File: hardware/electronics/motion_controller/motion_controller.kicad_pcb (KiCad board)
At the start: 2 copper layers, 266.7 x 95.3 mm, 186 parts, among them K1 CONN_3, K10 CONN_3, K11 CONN_3, K12 CONN_3, K13 CONN_3, K14 CONN_3, K15 CONN_3, K2 CONN_3, K3 CONN_3, K4 CONN_3, K5 CONN_3, K6 CONN_3, K7 CONN_3, K8 CONN_3, K9 CONN_3, P1 CONN_2, P10 CONN_4, P11 CONN_4, P12 CONN_4, P13 CONN_2, P14 CONN_2, P15 CONN_2, P16 CONN_2, P17 CONN_2, P18 CONN_2, P19 CONN_2X2, P2 CONN_5X2, P20 CONN_2X2, P21 CONN_2, P22 CONN_2, P23 CONN_2, P24 CONN_2, P25 CONN_2, P26 CONN_2X2, P27 CONN_2, P28 CONN_2, P29 CONN_2, P3 CONN_2X2, P30 CONN_1, P31 CONN_1, P32 CONN_1, P33 CONN_1, P4 CONN_2, P5 CONN_34X2, P6 CONN_4, P7 CONN_4, P8 CONN_4, P9 CONN_4, U1 TEENSY3.X, U10 OP07, U11 OP07, U12 OP07, U13 OP07, U14 OP07, U15 OP07, U16 OP07, U17 MEA1D0512SC, U18 PJRC_SD_CARD, U2 NC7WZ04, U3 NC7WZ16, U4 NC7WZ16, U5 SSR_DC_6PIN, U6 MAX6176AASA+, U7 OP07, U8 OP07, U9 OP07

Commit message: Modified motion controller pcb slightly - made so that only one mounting hole is grounded.
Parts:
- U1: value TEENSY3.X -> TEENSY3.1
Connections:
- P30 pad 1: /GND -> (no net)
- P31 pad 1: /GND -> (no net)
- P32 pad 1: /GND -> (no net)
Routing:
- net /GND: track 789.9 -> 771.2 mm
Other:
- board text added: "ANALOG INPUTS"

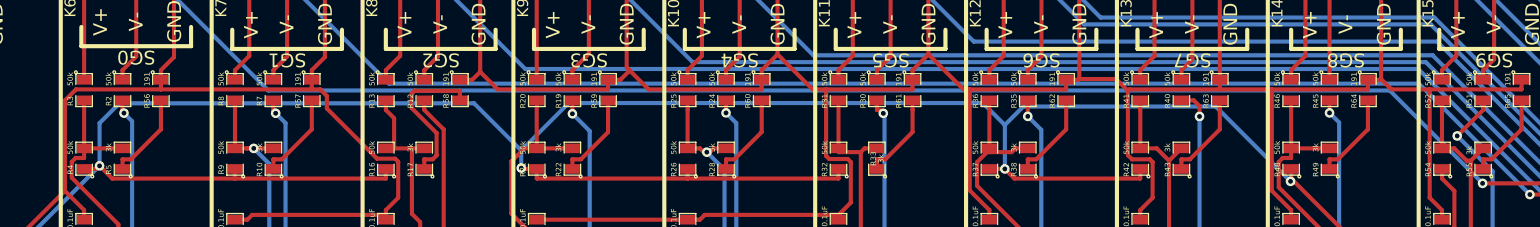
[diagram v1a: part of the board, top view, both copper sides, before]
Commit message: Worked on BOM for motion controller PCB.
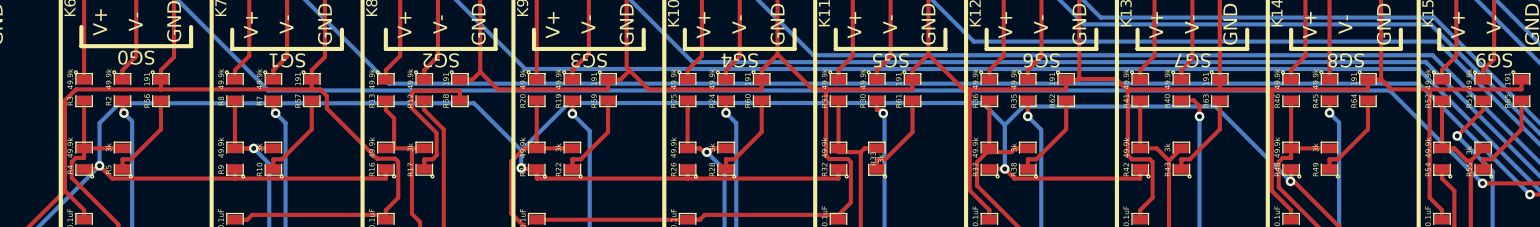
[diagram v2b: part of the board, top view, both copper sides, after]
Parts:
- R12, R13, R16, R19, R2, R20, R21, R24, R25, R26, R3, R30, R31, R32, R35, R36, R37, R4, R40, R41, R42, R45, R46, R48, R51, R52, R54, R7, R8, R9: value 50k -> 49.9k

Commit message: Added sympy derivation of differential amplifier gain for motion controller pcb.
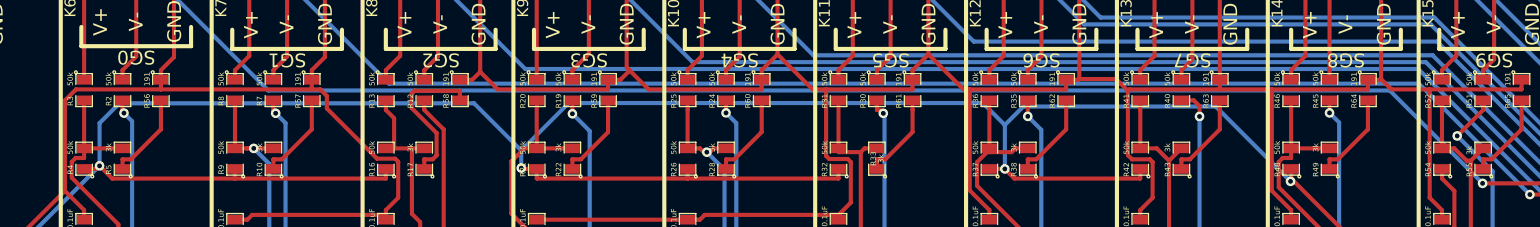
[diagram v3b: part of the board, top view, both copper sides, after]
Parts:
- R12, R13, R16, R19, R2, R20, R21, R24, R25, R26, R3, R30, R31, R32, R35, R36, R37, R4, R40, R41, R42, R45, R46, R48, R51, R52, R54, R7, R8, R9: value 49.9k -> 50k
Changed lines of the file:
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@@
       (effects (font (size 0.50038 0.50038) (thickness 0.10922)))
     )
-    (fp_text value 49.9k (at -1.016 1.27 270) (layer F.SilkS)
+    (fp_text value 50k (at -1.016 1.27 270) (layer F.SilkS)
       (effects (font (size 0.50038 0.50038) (thickness 0.10922)))
     )
@@
       (effects (font (size 0.50038 0.50038) (thickness 0.10922)))
     )
-    (fp_text value 49.9k (at -1.016 1.27 270) (layer F.SilkS)
+    (fp_text value 50k (at -1.016 1.27 270) (layer F.SilkS)
       (effects (font (size 0.50038 0.50038) (thickness 0.10922)))
     )
@@
       (effects (font (size 0.50038 0.50038) (thickness 0.10922)))
     )
-    (fp_text value 49.9k (at 1.016 -1.27 90) (layer F.SilkS)
+    (fp_text value 50k (at 1.016 -1.27 90) (layer F.SilkS)
       (effects (font (size 0.50038 0.50038) (thickness 0.10922)))
     )
@@
       (effects (font (size 0.50038 0.50038) (thickness 0.10922)))
     )
-    (fp_text value 49.9k (at 1.016 -1.27 90) (layer F.SilkS)
+    (fp_text value 50k (at 1.016 -1.27 90) (layer F.SilkS)
       (effects (font (size 0.50038 0.50038) (thickness 0.10922)))
     )
@@
       (effects (font (size 0.50038 0.50038) (thickness 0.10922)))
     )
-    (fp_text value 49.9k (at -1.016 1.27 270) (layer F.SilkS)
+    (fp_text value 50k (at -1.016 1.27 270) (layer F.SilkS)
       (effects (font (size 0.50038 0.50038) (thickness 0.10922)))
     )
@@
       (effects (font (size 0.50038 0.50038) (thickness 0.10922)))
     )
-    (fp_text value 49.9k (at -1.016 1.27 270) (layer F.SilkS)
+    (fp_text value 50k (at -1.016 1.27 270) (layer F.SilkS)
       (effects (font (size 0.50038 0.50038) (thickness 0.10922)))
     )
@@
       (effects (font (size 0.50038 0.50038) (thickness 0.10922)))
     )
-    (fp_text value 49.9k (at 1.016 -1.27 90) (layer F.SilkS)
+    (fp_text value 50k (at 1.016 -1.27 90) (layer F.SilkS)
       (effects (font (size 0.50038 0.50038) (thickness 0.10922)))
     )
@@
       (effects (font (size 0.50038 0.50038) (thickness 0.10922)))
     )
-    (fp_text value 49.9k (at -1.016 1.27 270) (layer F.SilkS)
+    (fp_text value 50k (at -1.016 1.27 270) (layer F.SilkS)
       (effects (font (size 0.50038 0.50038) (thickness 0.10922)))
     )
@@
       (effects (font (size 0.50038 0.50038) (thickness 0.10922)))
     )
-    (fp_text value 49.9k (at -1.016 1.27 270) (layer F.SilkS)
+    (fp_text value 50k (at -1.016 1.27 270) (layer F.SilkS)
       (effects (font (size 0.50038 0.50038) (thickness 0.10922)))
     )
@@
       (effects (font (size 0.50038 0.50038) (thickness 0.10922)))
     )
-    (fp_text value 49.9k (at 1.016 -1.27 90) (layer F.SilkS)
+    (fp_text value 50k (at 1.016 -1.27 90) (layer F.SilkS)
       (effects (font (size 0.50038 0.50038) (thickness 0.10922)))
     )
@@
       (effects (font (size 0.50038 0.50038) (thickness 0.10922)))
     )
-    (fp_text value 49.9k (at -1.016 1.27 270) (layer F.SilkS)
+    (fp_text value 50k (at -1.016 1.27 270) (layer F.SilkS)
       (effects (font (size 0.50038 0.50038) (thickness 0.10922)))
     )
@@
       (effects (font (size 0.50038 0.50038) (thickness 0.10922)))
     )
-    (fp_text value 49.9k (at -1.016 1.27 270) (layer F.SilkS)
+    (fp_text value 50k (at -1.016 1.27 270) (layer F.SilkS)
       (effects (font (size 0.50038 0.50038) (thickness 0.10922)))
     )
@@
       (effects (font (size 0.50038 0.50038) (thickness 0.10922)))
     )
-    (fp_text value 49.9k (at 1.016 -1.27 90) (layer F.SilkS)
+    (fp_text value 50k (at 1.016 -1.27 90) (layer F.SilkS)
       (effects (font (size 0.50038 0.50038) (thickness 0.10922)))
     )
@@
       (effects (font (size 0.50038 0.50038) (thickness 0.10922)))
     )
-    (fp_text value 49.9k (at -1.016 1.27 270) (layer F.SilkS)
+    (fp_text value 50k (at -1.016 1.27 270) (layer F.SilkS)
       (effects (font (size 0.50038 0.50038) (thickness 0.10922)))
     )
@@
       (effects (font (size 0.50038 0.50038) (thickness 0.10922)))
     )
-    (fp_text value 49.9k (at -1.016 1.27 270) (layer F.SilkS)
+    (fp_text value 50k (at -1.016 1.27 270) (layer F.SilkS)
       (effects (font (size 0.50038 0.50038) (thickness 0.10922)))
     )
@@
       (effects (font (size 0.50038 0.50038) (thickness 0.10922)))
     )
-    (fp_text value 49.9k (at 1.016 -1.27 90) (layer F.SilkS)
+    (fp_text value 50k (at 1.016 -1.27 90) (layer F.SilkS)
       (effects (font (size 0.50038 0.50038) (thickness 0.10922)))
     )
@@
       (effects (font (size 0.50038 0.50038) (thickness 0.10922)))
     )
-    (fp_text value 49.9k (at -1.016 1.27 270) (layer F.SilkS)
+    (fp_text value 50k (at -1.016 1.27 270) (layer F.SilkS)
       (effects (font (size 0.50038 0.50038) (thickness 0.10922)))
     )
@@
       (effects (font (size 0.50038 0.50038) (thickness 0.10922)))
     )
-    (fp_text value 49.9k (at -1.016 1.27 270) (layer F.SilkS)
+    (fp_text value 50k (at -1.016 1.27 270) (layer F.SilkS)
       (effects (font (size 0.50038 0.50038) (thickness 0.10922)))
     )
@@
       (effects (font (size 0.50038 0.50038) (thickness 0.10922)))
     )
-    (fp_text value 49.9k (at 1.016 -1.27 90) (layer F.SilkS)
+    (fp_text value 50k (at 1.016 -1.27 90) (layer F.SilkS)
       (effects (font (size 0.50038 0.50038) (thickness 0.10922)))
     )
@@
       (effects (font (size 0.50038 0.50038) (thickness 0.10922)))
     )
-    (fp_text value 49.9k (at -1.016 1.27 270) (layer F.SilkS)
+    (fp_text value 50k (at -1.016 1.27 270) (layer F.SilkS)
       (effects (font (size 0.50038 0.50038) (thickness 0.10922)))
     )
@@
       (effects (font (size 0.50038 0.50038) (thickness 0.10922)))
     )
-    (fp_text value 49.9k (at -1.016 1.27 270) (layer F.SilkS)
+    (fp_text value 50k (at -1.016 1.27 270) (layer F.SilkS)
       (effects (font (size 0.50038 0.50038) (thickness 0.10922)))
     )
@@
       (effects (font (size 0.50038 0.50038) (thickness 0.10922)))
     )
-    (fp_text value 49.9k (at -1.016 1.27 270) (layer F.SilkS)
+    (fp_text value 50k (at -1.016 1.27 270) (layer F.SilkS)
       (effects (font (size 0.50038 0.50038) (thickness 0.10922)))
     )
@@
       (effects (font (size 0.50038 0.50038) (thickness 0.10922)))
     )
-    (fp_text value 49.9k (at 1.016 -1.27 90) (layer F.SilkS)
+    (fp_text value 50k (at 1.016 -1.27 90) (layer F.SilkS)
       (effects (font (size 0.50038 0.50038) (thickness 0.10922)))
     )
@@
       (effects (font (size 0.50038 0.50038) (thickness 0.10922)))
     )
-    (fp_text value 49.9k (at -1.016 1.27 270) (layer F.SilkS)
+    (fp_text value 50k (at -1.016 1.27 270) (layer F.SilkS)
       (effects (font (size 0.50038 0.50038) (thickness 0.10922)))
     )
@@
       (effects (font (size 0.50038 0.50038) (thickness 0.10922)))
     )
-    (fp_text value 49.9k (at -1.016 1.27 270) (layer F.SilkS)
+    (fp_text value 50k (at -1.016 1.27 270) (layer F.SilkS)
       (effects (font (size 0.50038 0.50038) (thickness 0.10922)))
     )
@@
       (effects (font (size 0.50038 0.50038) (thickness 0.10922)))
     )
-    (fp_text value 49.9k (at 1.016 -1.27 90) (layer F.SilkS)
+    (fp_text value 50k (at 1.016 -1.27 90) (layer F.SilkS)
       (effects (font (size 0.50038 0.50038) (thickness 0.10922)))
     )
@@
       (effects (font (size 0.50038 0.50038) (thickness 0.10922)))
     )
-    (fp_text value 49.9k (at -1.016 1.27 270) (layer F.SilkS)
+    (fp_text value 50k (at -1.016 1.27 270) (layer F.SilkS)
       (effects (font (size 0.50038 0.50038) (thickness 0.10922)))
     )
@@
       (effects (font (size 0.50038 0.50038) (thickness 0.10922)))
     )
-    (fp_text value 49.9k (at -1.016 1.27 270) (layer F.SilkS)
+    (fp_text value 50k (at -1.016 1.27 270) (layer F.SilkS)
       (effects (font (size 0.50038 0.50038) (thickness 0.10922)))
     )
@@
       (effects (font (size 0.50038 0.50038) (thickness 0.10922)))
     )
-    (fp_text value 49.9k (at -1.016 1.27 270) (layer F.SilkS)
+    (fp_text value 50k (at -1.016 1.27 270) (layer F.SilkS)
       (effects (font (size 0.50038 0.50038) (thickness 0.10922)))
     )
@@
       (effects (font (size 0.50038 0.50038) (thickness 0.10922)))
     )
-    (fp_text value 49.9k (at 1.016 -1.27 90) (layer F.SilkS)
+    (fp_text value 50k (at 1.016 -1.27 90) (layer F.SilkS)
       (effects (font (size 0.50038 0.50038) (thickness 0.10922)))
     )
